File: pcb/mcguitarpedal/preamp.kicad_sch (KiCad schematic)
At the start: 33 parts, among them SW1 LINE_LEVEL, U1 LM4562, U2 Teensy4.1, U3 Teensy4.0_AudioShield_REVD

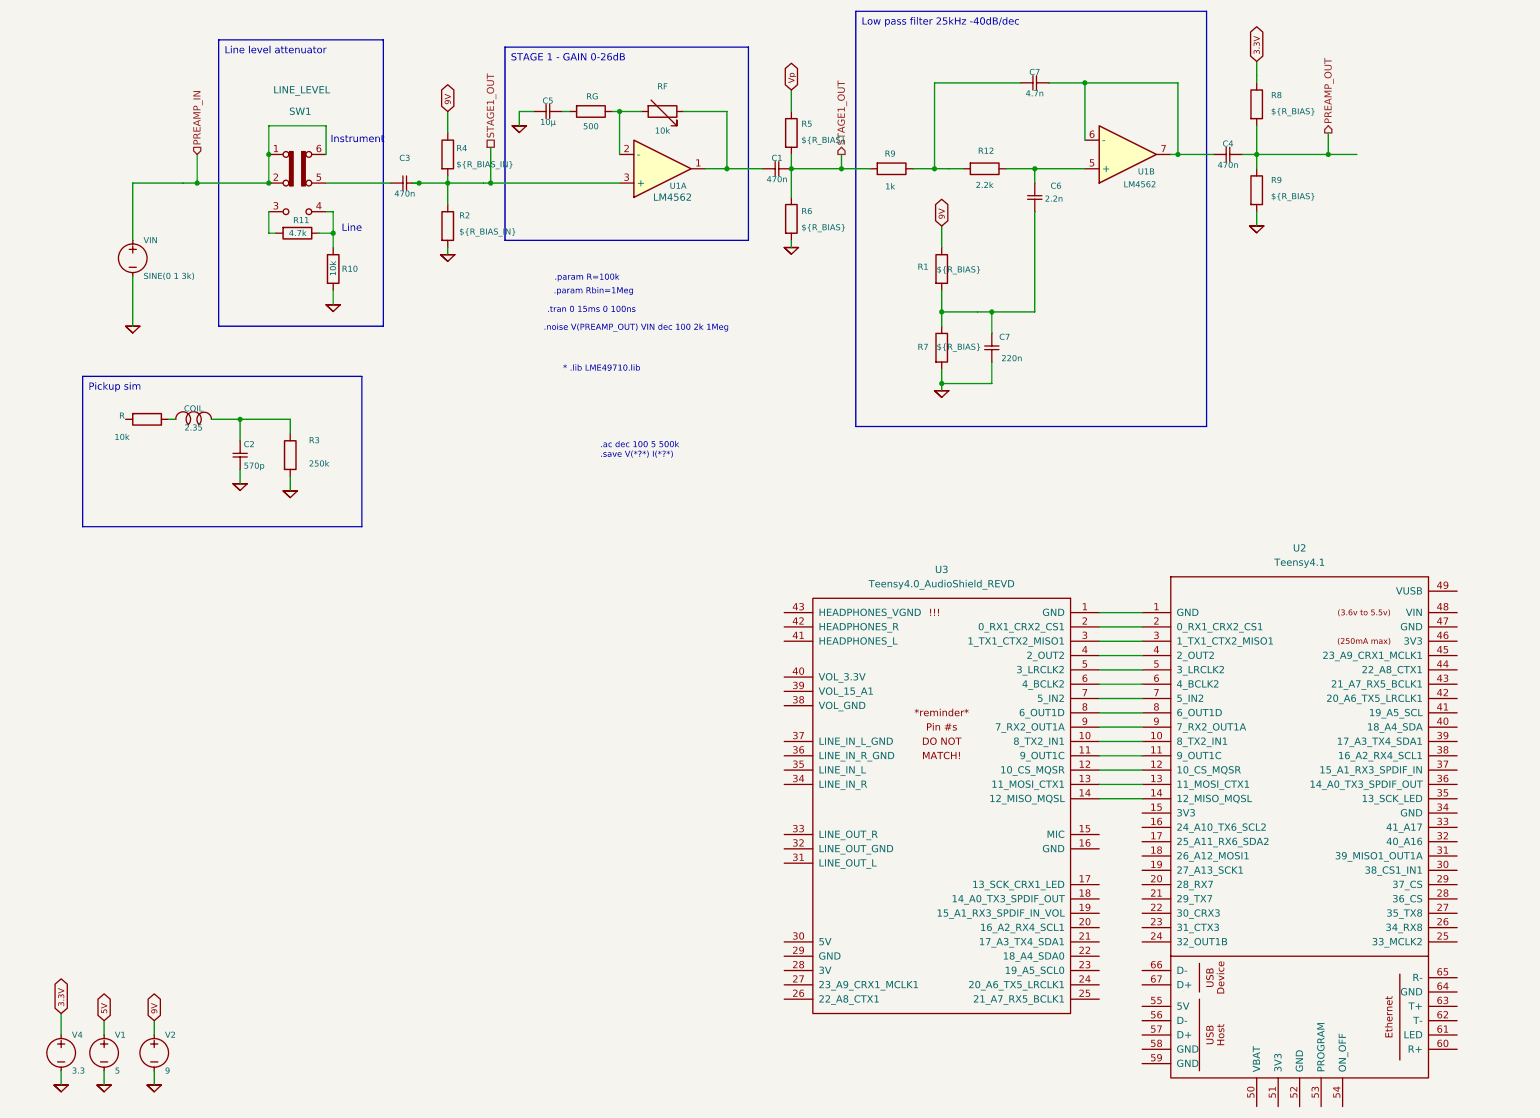
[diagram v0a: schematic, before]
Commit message: Teensy symbol libraries
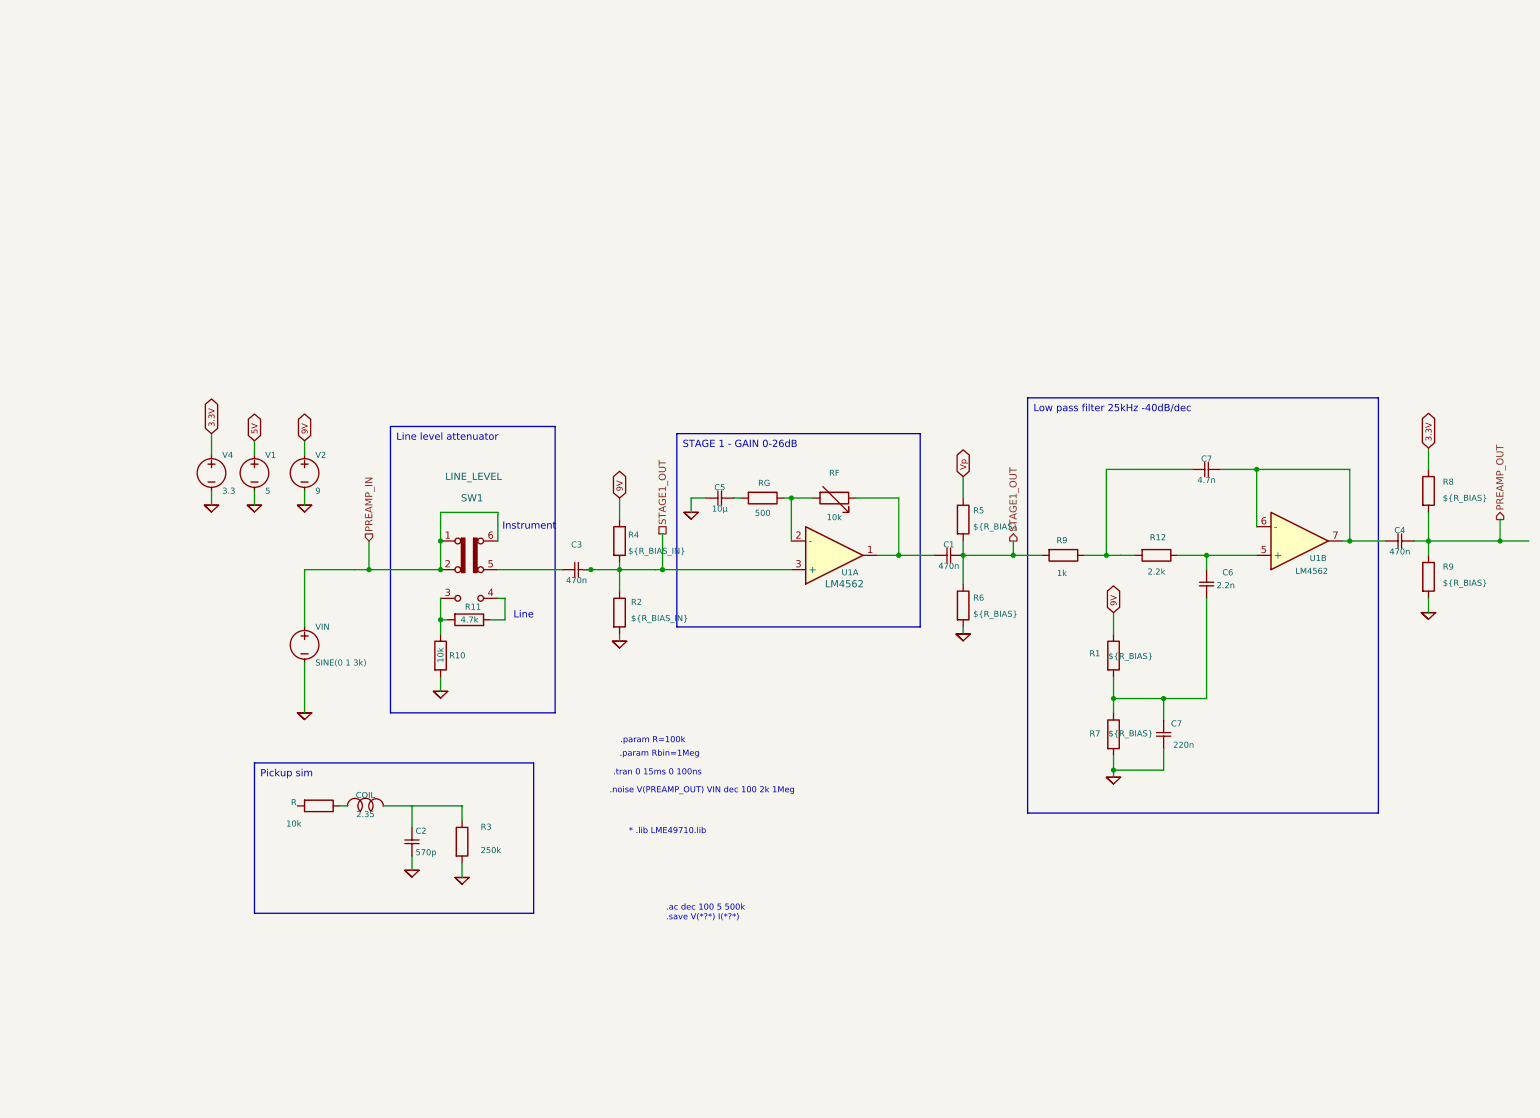
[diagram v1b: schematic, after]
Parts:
- removed U2: Teensy4.1, symbol Teensy:Teensy4.1
- removed U3: Teensy4.0_AudioShield_REVD, symbol Audio board:Teensy4.0_AudioShield_REVD
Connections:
- net at R11.1, SW1.4 (A): no longer R10.1
- net at R11.2, SW1.3 (C): now also R10.1
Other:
- moved on the sheet: C1, C2, C3, C4, C5, C6, C7, COIL, R, R1, R10, R11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

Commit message: Schematic symbols
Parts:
- removed C2: 570p, symbol ltspice:cap
- removed COIL: 2.35, symbol ltspice:ind
- removed R: 10k, symbol Device:R
- removed R3: 250k, symbol Device:R
- removed V1: 5, symbol ltspice:voltage
- removed V2: 9, symbol ltspice:voltage
- removed V4: 3.3, symbol ltspice:voltage
- added V?: 5, symbol ltspice:voltage
- added V?: 3.3, symbol ltspice:voltage
- added V?: 9, symbol ltspice:voltage
- renumbered C6 to C5, C7 to C6, C7 to C?, C3 to C?, C5 to C?, C1 to C?, C4 to C?, R12 to R10, R9 to R7, R2 to R?, R10 to R?, R8 to R?, R1 to R?, R5 to R?, R6 to R?, R9 to R?, R4 to R?, R11 to R?, R7 to R?, RF to RF?, RG to RG?, SW1 to SW?, U1 to U3, U1 to U?, VIN to VIN?
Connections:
- net 0: now also V?.2 (-), V?.2 (-), V?.2 (-)
- net 3.3V: now also V?.1 (+)
- net 5V: now also V?.1 (+)
- net 9V: now also V?.1 (+)
- net STAGE1_OUT: no longer C?.1, R?.1, R?.2, U?.3 (+)
- new net STAGE1_IN: C?.1, R?.1, R?.2, U?.3 (+)

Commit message: ILI9488 schematic
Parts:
- removed V?: 5, symbol ltspice:voltage
- removed V?: 3.3, symbol ltspice:voltage
- removed V?: 9, symbol ltspice:voltage
- removed VIN?: SINE(0 1 3k), symbol ltspice:voltage
- added unit 3 of U3
- C5: footprint (none) -> Capacitor_THT:C_Rect_L7.5mm_W6.5mm_P5.00mm
- C6: footprint (none) -> Capacitor_THT:C_Rect_L7.2mm_W7.2mm_P5.00mm_FKS2_FKP2_MKS2_MKP2
- C?: footprint (none) -> Capacitor_THT:C_Rect_L7.2mm_W2.5mm_P5.00mm_FKS2_FKP2_MKS2_MKP2
- C? (x3): footprint (none) -> Capacitor_THT:C_Rect_L18.0mm_W11.0mm_P15.00mm_FKS3_FKP3
- C?: footprint (none) -> Capacitor_THT:CP_Radial_D6.3mm_P2.50mm
- R10, R7, R? (x10), RF?, RG?: footprint (none) -> Resistor_THT:R_Axial_DIN0207_L6.3mm_D2.5mm_P7.62mm_Horizontal
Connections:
- net 9V: now also U3.8 (V+)
- new net GND: U3.4 (V-)

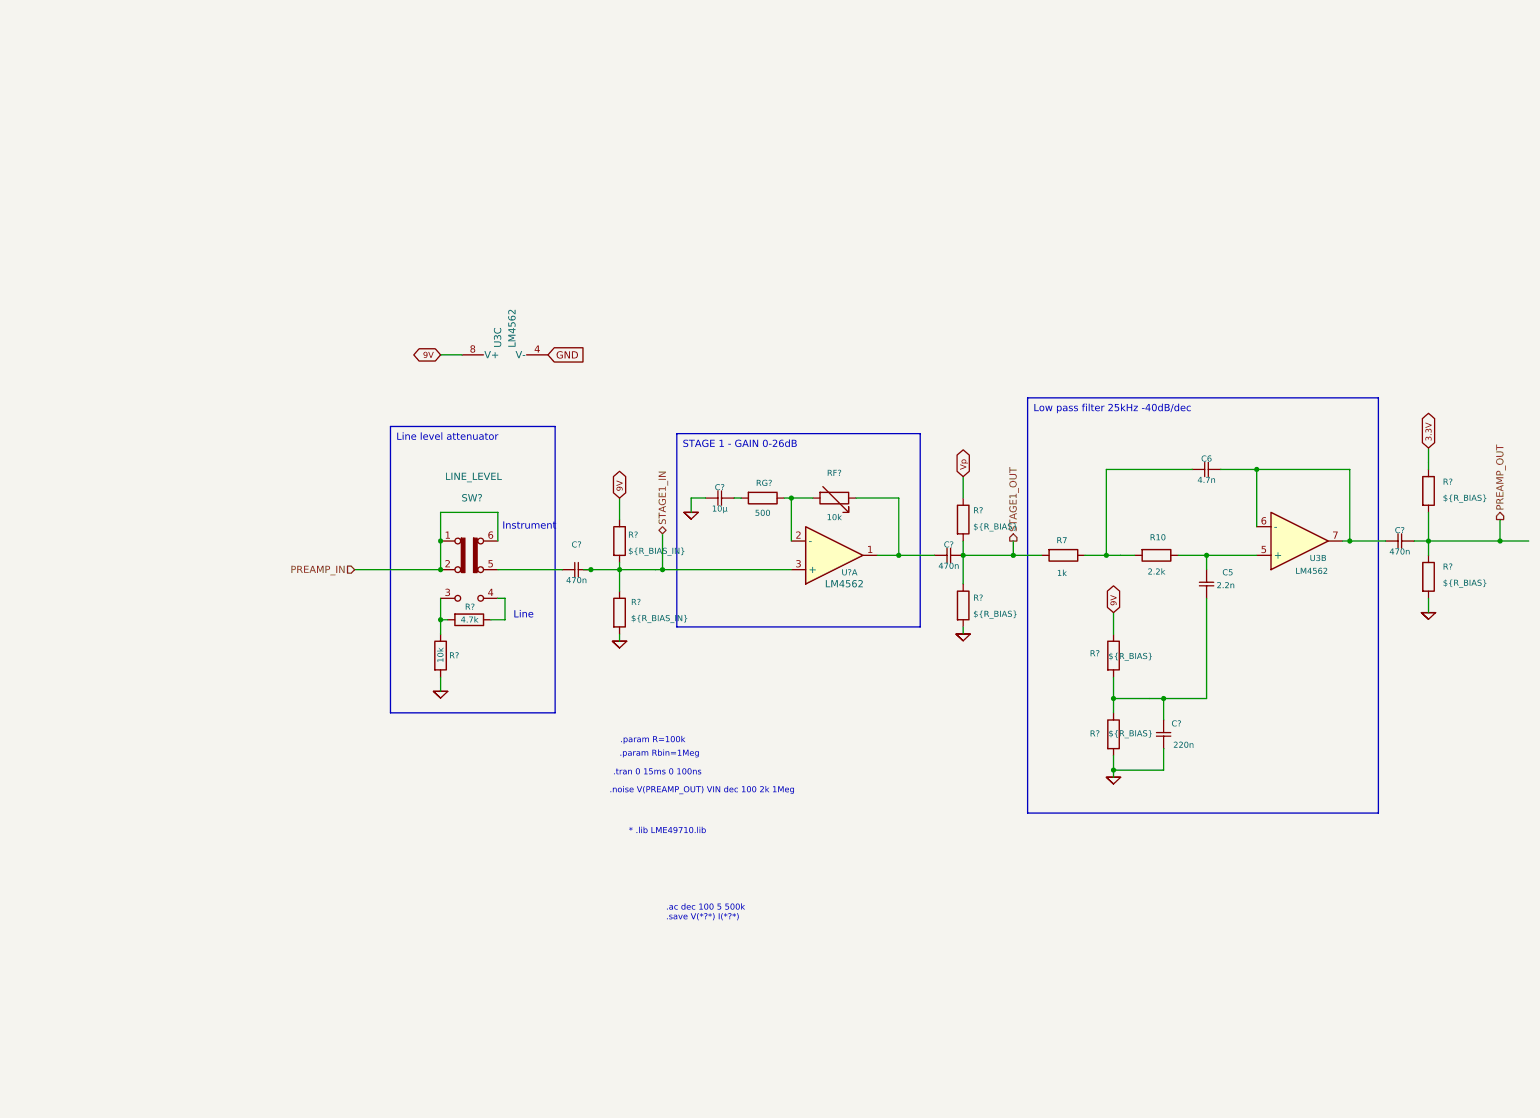
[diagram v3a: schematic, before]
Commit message: PCB physical layout
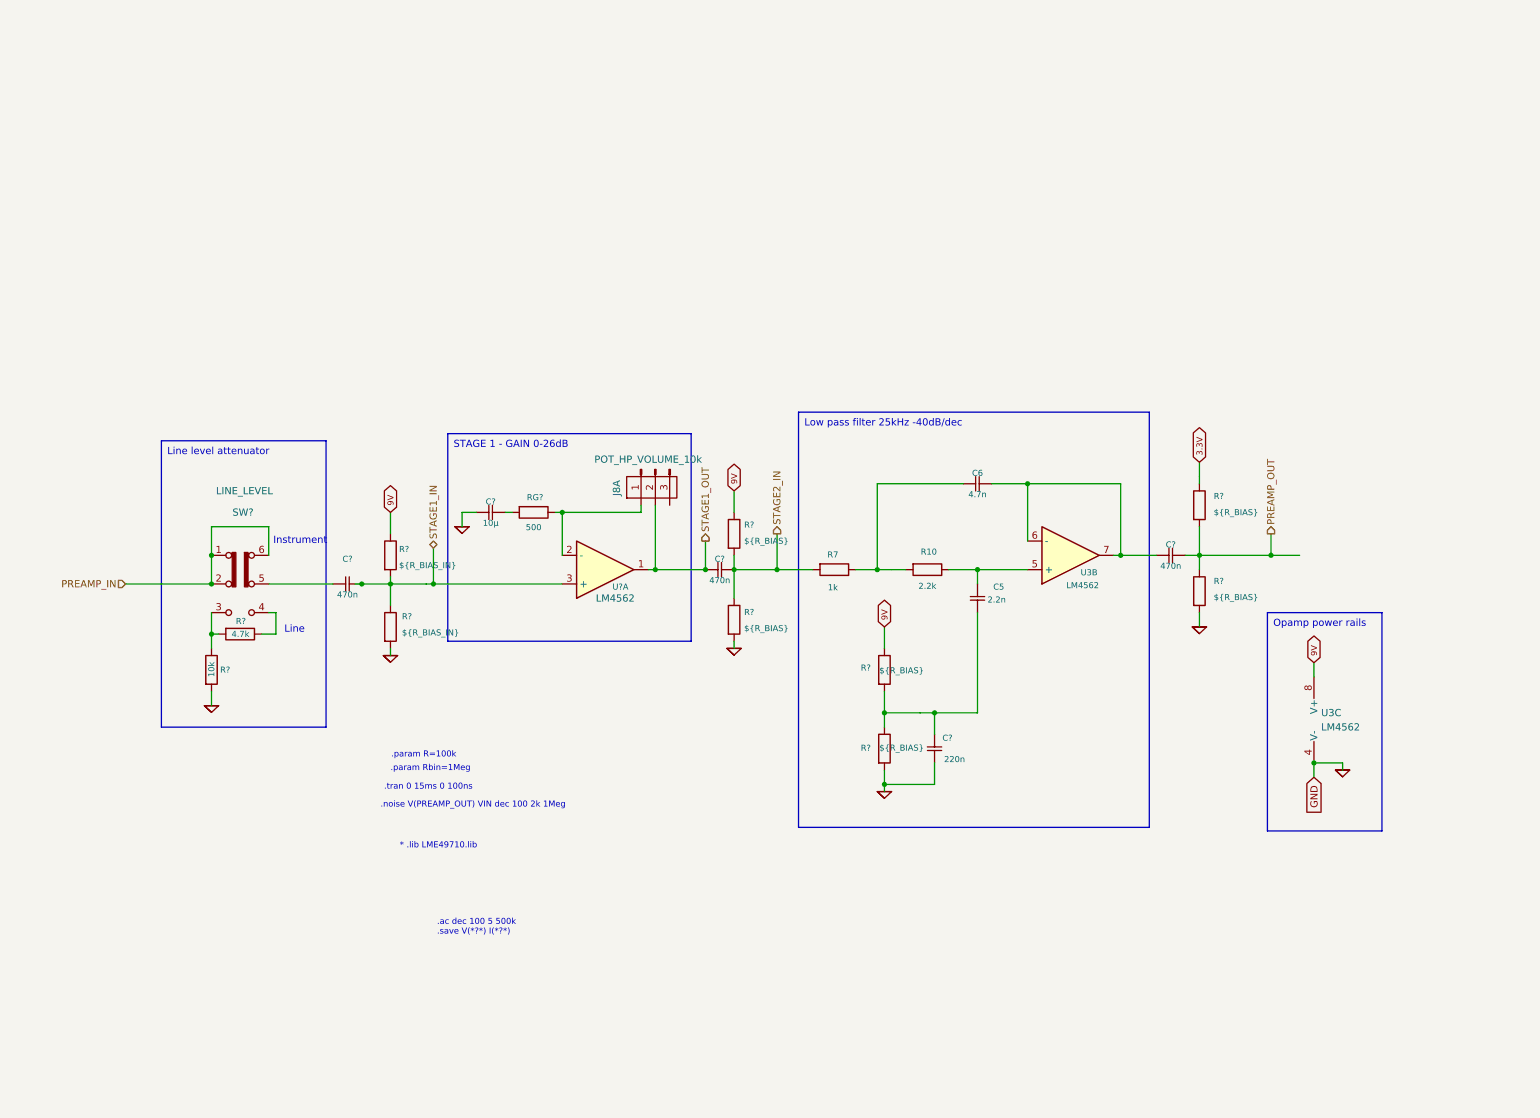
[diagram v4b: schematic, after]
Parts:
- removed RF?: 10k, Resistor_THT:R_Axial_DIN0207_L6.3mm_D2.5mm_P7.62mm_Horizontal, symbol Device:R_Variable
- added J8: POT_HP_VOLUME_10k, Connector_PinHeader_2.54mm:PinHeader_1x09_P2.54mm_Vertical, symbol mcguitarpedal:3x2_Headers
- C? (x3): footprint Capacitor_THT:C_Rect_L18.0mm_W11.0mm_P15.00mm_FKS3_FKP3 -> Capacitor_THT:C_Rect_L18.0mm_W5.0mm_P15.00mm_FKS3_FKP3
- SW?: footprint (none) -> Button_Switch_THT:SW_CK_JS202011AQN_DPDT_Angled
- U3: footprint (none) -> LM4562:lm4562
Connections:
- net GND is gone; now on net 0: U3.4 (V-)
- net Vp is gone; now on net 9V: R?.1
- net STAGE1_OUT: now also C?.2, U?.1, J8.2 (Pin_2); no longer C?.1, R7.2, R?.1, R?.2
- net at RG?.1, U?.2 (-): now also J8.1 (Pin_1)
- new net STAGE2_IN: C?.1, R7.2, R?.1, R?.2
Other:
- moved on the sheet: C5, C6, C?, R10, R7, R?, RG?, SW?, U3B, U3C, U?A
